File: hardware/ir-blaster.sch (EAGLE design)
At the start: 10 parts, among them Q1 BC547

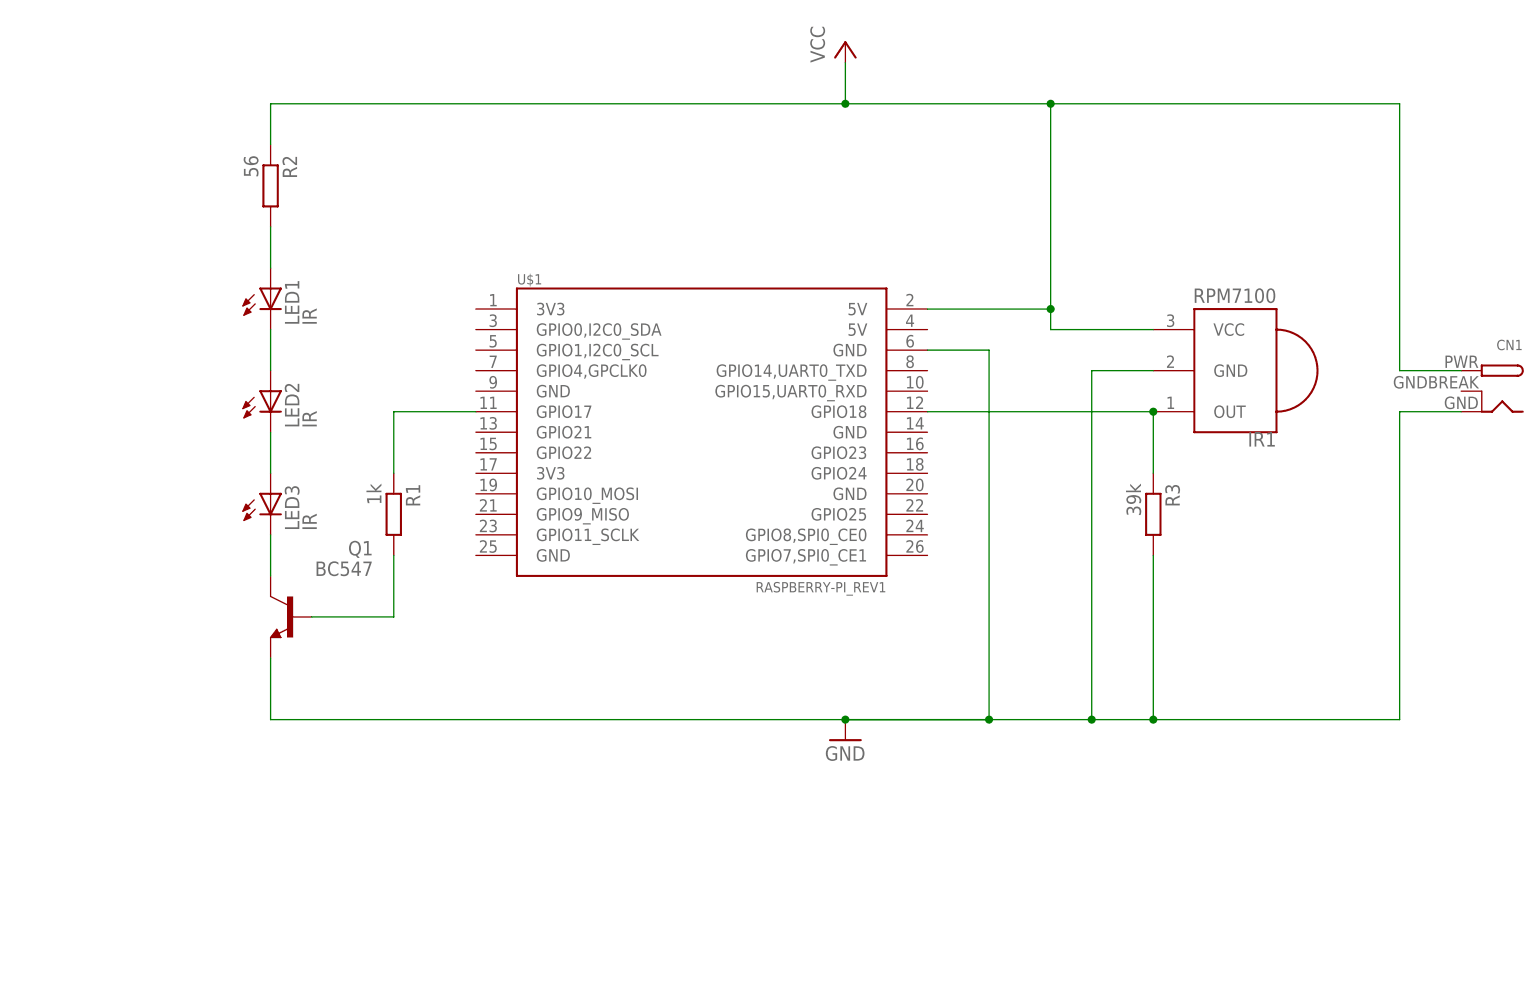
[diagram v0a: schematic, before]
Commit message: Revision 3. Moved the LEDs off board onto wires
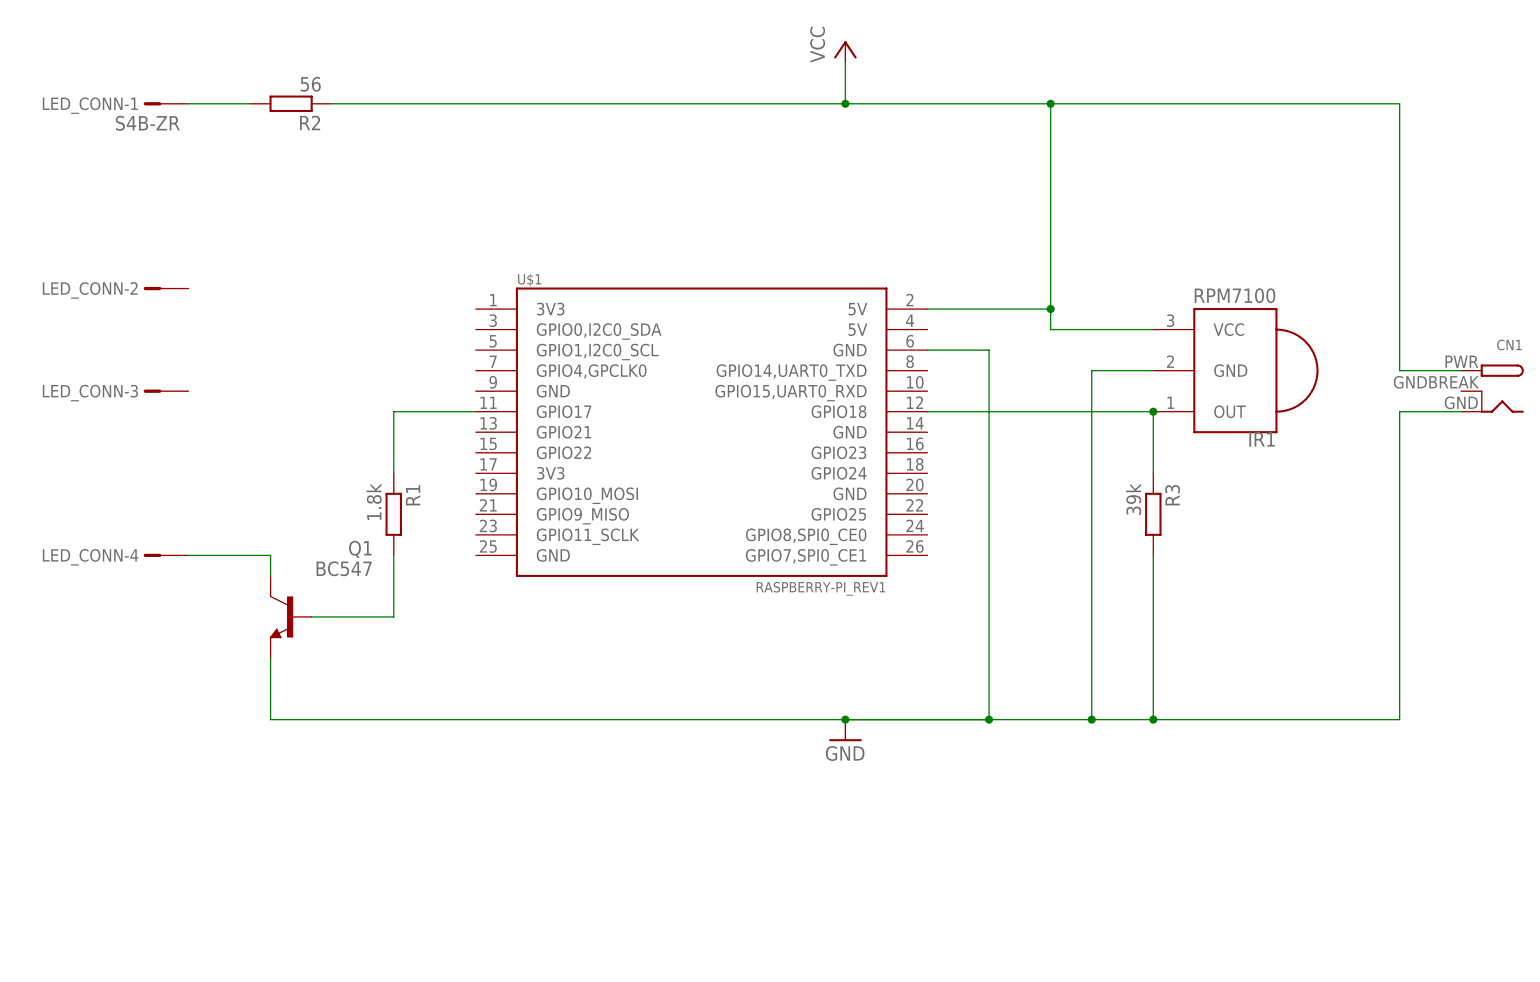
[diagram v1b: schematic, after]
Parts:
- removed LED1, LED2, LED3: IR, eagle-ltspice:LED_ELD260
- added LED_CONN: S4B-ZR, con-jst:S4B-ZR
- R1: value 1k -> 1.8k
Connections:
- removed net N$3: LED1.C, LED2.A
- removed net N$4: LED2.C, LED3.A
- net N$1: now also LED_CONN-1.1, R2.2; no longer LED3.C, Q1.C
- net N$2: now also LED_CONN-4.1, Q1.C; no longer LED1.A, R2.2
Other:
- moved on the sheet: R2
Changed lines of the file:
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@@
 <?xml version="1.0" encoding="utf-8"?>
 <!DOCTYPE eagle SYSTEM "eagle.dtd">
-<eagle version="7.5.0">
+<eagle version="8.0.2">
 <drawing>
 <settings>
@@
 <parts>
 <part name="Q1" library="transistor" deviceset="BC547" device=""/>
-<part name="LED1" library="eagle-ltspice" deviceset="LED_E" device="LD260" value="IR"/>
-<part name="LED2" library="eagle-ltspice" deviceset="LED_E" device="LD260" value="IR"/>
-<part name="LED3" library="eagle-ltspice" deviceset="LED_E" device="LD260" value="IR"/>
-<part name="R1" library="eagle-ltspice" deviceset="R" device="0207/10" value="1k"/>
+<part name="R1" library="eagle-ltspice" deviceset="R" device="0207/10" value="1.8k"/>
 <part name="R2" library="eagle-ltspice" deviceset="R" device="0207/10" value="56"/>
 <part name="GND1" library="supply1" deviceset="GND" device=""/>
@@
 <part name="U$1" library="RaspberryPi" deviceset="RASPBERRY-PI_REV1" device=""/>
 <part name="CN1" library="adafruit" deviceset="DCBARREL" device="PTH"/>
+<part name="LED_CONN" library="con-jst" deviceset="?4B-ZR" device="S"/>
 </parts>
 <sheets>
@@
 <instances>
 <instance part="Q1" gate="G$1" x="-58.42" y="55.88" rot="MR0"/>
-<instance part="LED1" gate="G$1" x="-60.96" y="96.52"/>
-<instance part="LED2" gate="G$1" x="-60.96" y="83.82"/>
-<instance part="LED3" gate="G$1" x="-60.96" y="71.12"/>
 <instance part="R1" gate="G$1" x="-45.72" y="68.58" rot="R270"/>
-<instance part="R2" gate="G$1" x="-60.96" y="109.22" rot="R270"/>
+<instance part="R2" gate="G$1" x="-58.42" y="119.38" rot="R180"/>
 <instance part="GND1" gate="1" x="10.16" y="40.64"/>
 <instance part="P+1" gate="VCC" x="10.16" y="127"/>
@@
 <instance part="U$1" gate="G$1" x="-7.62" y="78.74"/>
 <instance part="CN1" gate="G$1" x="88.9" y="83.82" rot="MR0"/>
+<instance part="LED_CONN" gate="-1" x="-76.2" y="119.38" rot="R180"/>
+<instance part="LED_CONN" gate="-2" x="-76.2" y="96.52" rot="R180"/>
+<instance part="LED_CONN" gate="-3" x="-76.2" y="83.82" rot="R180"/>
+<instance part="LED_CONN" gate="-4" x="-76.2" y="63.5" rot="R180"/>
 </instances>
 <busses>
 </busses>
 <nets>
-<net name="N$3" class="0">
-<segment>
-<pinref part="LED1" gate="G$1" pin="C"/>
-<pinref part="LED2" gate="G$1" pin="A"/>
-<wire x1="-60.96" y1="91.44" x2="-60.96" y2="86.36" width="0.1524" layer="91"/>
-</segment>
-</net>
-<net name="N$4" class="0">
-<segment>
-<pinref part="LED2" gate="G$1" pin="C"/>
-<pinref part="LED3" gate="G$1" pin="A"/>
-<wire x1="-60.96" y1="78.74" x2="-60.96" y2="73.66" width="0.1524" layer="91"/>
-</segment>
-</net>
 <net name="GND" class="0">
 <segment>
@@
 <junction x="35.56" y="119.38"/>
 <pinref part="R2" gate="G$1" pin="1"/>
-<wire x1="-60.96" y1="114.3" x2="-60.96" y2="119.38" width="0.1524" layer="91"/>
-<wire x1="-60.96" y1="119.38" x2="10.16" y2="119.38" width="0.1524" layer="91"/>
+<wire x1="-53.34" y1="119.38" x2="10.16" y2="119.38" width="0.1524" layer="91"/>
 <junction x="10.16" y="119.38"/>
 <wire x1="78.74" y1="119.38" x2="78.74" y2="86.36" width="0.1524" layer="91"/>
 <pinref part="CN1" gate="G$1" pin="PWR"/>
 <wire x1="78.74" y1="86.36" x2="86.36" y2="86.36" width="0.1524" layer="91"/>
-</segment>
-</net>
-<net name="N$1" class="0">
-<segment>
-<pinref part="LED3" gate="G$1" pin="C"/>
-<pinref part="Q1" gate="G$1" pin="C"/>
-<wire x1="-60.96" y1="66.04" x2="-60.96" y2="60.96" width="0.1524" layer="91"/>
-</segment>
-</net>
-<net name="N$2" class="0">
-<segment>
-<pinref part="LED1" gate="G$1" pin="A"/>
-<pinref part="R2" gate="G$1" pin="2"/>
-<wire x1="-60.96" y1="99.06" x2="-60.96" y2="104.14" width="0.1524" layer="91"/>
 </segment>
 </net>
@@
 </segment>
 </net>
+<net name="N$1" class="0">
+<segment>
+<pinref part="LED_CONN" gate="-1" pin="1"/>
+<pinref part="R2" gate="G$1" pin="2"/>
+<wire x1="-71.12" y1="119.38" x2="-63.5" y2="119.38" width="0.1524" layer="91"/>
+</segment>
+</net>
+<net name="N$2" class="0">
+<segment>
+<pinref part="LED_CONN" gate="-4" pin="1"/>
+<pinref part="Q1" gate="G$1" pin="C"/>
+<wire x1="-71.12" y1="63.5" x2="-60.96" y2="63.5" width="0.1524" layer="91"/>
+<wire x1="-60.96" y1="63.5" x2="-60.96" y2="60.96" width="0.1524" layer="91"/>
+</segment>
+</net>

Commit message: Adding pads for the USB wifi dongle
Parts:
- added X1: KUSBVX, con-kycon-no-mask:KUSBVX
- added X2: (no value), con-yamaichi-no-mask:USB-A003
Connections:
- new net N$3: X1.1, X2.1
- new net N$4: X1.2, X2.2
- new net N$8: X1.3, X2.3
- new net N$9: X1.4, X2.4
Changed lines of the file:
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@@
 <part name="CN1" library="adafruit" deviceset="DCBARREL" device="PTH"/>
 <part name="LED_CONN" library="con-jst" deviceset="?4B-ZR" device="S"/>
+<part name="X2" library="con-yamaichi-no-mask" deviceset="USB-A003" device=""/>
+<part name="X1" library="con-kycon-no-mask" deviceset="KUSBVX" device=""/>
 </parts>
 <sheets>
@@
 <instance part="LED_CONN" gate="-3" x="-76.2" y="83.82" rot="R180"/>
 <instance part="LED_CONN" gate="-4" x="-76.2" y="63.5" rot="R180"/>
+<instance part="X2" gate="G$1" x="-50.8" y="20.32" rot="MR0"/>
+<instance part="X1" gate="G$1" x="-35.56" y="20.32"/>
 </instances>
 <busses>
@@
 </segment>
 </net>
+<net name="N$3" class="0">
+<segment>
+<pinref part="X2" gate="G$1" pin="1"/>
+<pinref part="X1" gate="G$1" pin="1"/>
+<wire x1="-45.72" y1="25.4" x2="-40.64" y2="25.4" width="0.1524" layer="91"/>
+</segment>
+</net>
+<net name="N$4" class="0">
+<segment>
+<pinref part="X2" gate="G$1" pin="2"/>
+<pinref part="X1" gate="G$1" pin="2"/>
+<wire x1="-45.72" y1="22.86" x2="-40.64" y2="22.86" width="0.1524" layer="91"/>
+</segment>
+</net>
+<net name="N$8" class="0">
+<segment>
+<pinref part="X2" gate="G$1" pin="3"/>
+<pinref part="X1" gate="G$1" pin="3"/>
+<wire x1="-45.72" y1="20.32" x2="-40.64" y2="20.32" width="0.1524" layer="91"/>
+</segment>
+</net>
+<net name="N$9" class="0">
+<segment>
+<pinref part="X2" gate="G$1" pin="4"/>
+<pinref part="X1" gate="G$1" pin="4"/>
+<wire x1="-45.72" y1="17.78" x2="-40.64" y2="17.78" width="0.1524" layer="91"/>
+</segment>
+</net>

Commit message: Working on version 3 of the board
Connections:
- net N$1: now also LED_CONN-3.1
- net N$2: now also LED_CONN-2.1
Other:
- moved on the sheet: LED_CONN-2, LED_CONN-3
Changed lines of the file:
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@@
 <instance part="CN1" gate="G$1" x="88.9" y="83.82" rot="MR0"/>
 <instance part="LED_CONN" gate="-1" x="-76.2" y="119.38" rot="R180"/>
-<instance part="LED_CONN" gate="-2" x="-76.2" y="96.52" rot="R180"/>
-<instance part="LED_CONN" gate="-3" x="-76.2" y="83.82" rot="R180"/>
+<instance part="LED_CONN" gate="-2" x="-76.2" y="73.66" rot="R180"/>
+<instance part="LED_CONN" gate="-3" x="-76.2" y="104.14" rot="R180"/>
 <instance part="LED_CONN" gate="-4" x="-76.2" y="63.5" rot="R180"/>
 <instance part="X2" gate="G$1" x="-50.8" y="20.32" rot="MR0"/>
@@
 <pinref part="LED_CONN" gate="-1" pin="1"/>
 <pinref part="R2" gate="G$1" pin="2"/>
-<wire x1="-71.12" y1="119.38" x2="-63.5" y2="119.38" width="0.1524" layer="91"/>
+<wire x1="-71.12" y1="119.38" x2="-68.58" y2="119.38" width="0.1524" layer="91"/>
+<pinref part="LED_CONN" gate="-3" pin="1"/>
+<wire x1="-68.58" y1="119.38" x2="-63.5" y2="119.38" width="0.1524" layer="91"/>
+<wire x1="-71.12" y1="104.14" x2="-68.58" y2="104.14" width="0.1524" layer="91"/>
+<wire x1="-68.58" y1="104.14" x2="-68.58" y2="119.38" width="0.1524" layer="91"/>
+<junction x="-68.58" y="119.38"/>
 </segment>
 </net>
 <net name="N$2" class="0">
 <segment>
+<pinref part="Q1" gate="G$1" pin="C"/>
+<pinref part="LED_CONN" gate="-2" pin="1"/>
+<wire x1="-71.12" y1="73.66" x2="-60.96" y2="73.66" width="0.1524" layer="91"/>
+<wire x1="-60.96" y1="73.66" x2="-60.96" y2="63.5" width="0.1524" layer="91"/>
 <pinref part="LED_CONN" gate="-4" pin="1"/>
-<pinref part="Q1" gate="G$1" pin="C"/>
+<wire x1="-60.96" y1="63.5" x2="-60.96" y2="60.96" width="0.1524" layer="91"/>
 <wire x1="-71.12" y1="63.5" x2="-60.96" y2="63.5" width="0.1524" layer="91"/>
-<wire x1="-60.96" y1="63.5" x2="-60.96" y2="60.96" width="0.1524" layer="91"/>
+<junction x="-60.96" y="63.5"/>
 </segment>
 </net>
